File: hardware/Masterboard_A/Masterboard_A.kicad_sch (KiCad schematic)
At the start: 0 parts

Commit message: lv sensor extension board for master
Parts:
- added C11, C5: 220n, Capacitor_SMD:C_1206_3216Metric_Pad1.33x1.80mm_HandSolder, symbol Device:C_Small
- added C14: 10u, Capacitor_SMD:C_1206_3216Metric_Pad1.33x1.80mm_HandSolder, symbol Device:C_Small
- added C15, C3: 100n, Capacitor_SMD:C_1206_3216Metric_Pad1.33x1.80mm_HandSolder, symbol Device:C_Small
- added R7: 49.9k, Resistor_SMD:R_1206_3216Metric_Pad1.30x1.75mm_HandSolder, symbol Device:R_US
- added R8: 100k, Resistor_SMD:R_1206_3216Metric_Pad1.30x1.75mm_HandSolder, symbol Device:R_US
- added SW1: SW_Push, Button_Switch_SMD:SW_SPST_PTS645, symbol Switch:SW_Push
- added U1: MCU-MSM0G3507SPM, PM0064A-IPC_A, symbol zzLocalLibrary:MCU-MSM0G3507SPM
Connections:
- new net: C11.1, C5.1, U1.32 (VCORE)
- new net: R8.2, U1.42 (PA2_ROSC)
- new net +3.3V: C14.1, C15.1, R7.1, U1.40 (VDD)
- new net GND: C11.2, C14.2, C15.2, C3.2, C5.2, R8.1, SW1.2, U1.41 (VSS)
- new net MCU_RST: C3.1, R7.2, SW1.1, U1.38 (RST_N)
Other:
- note added: "MCU reset btn"

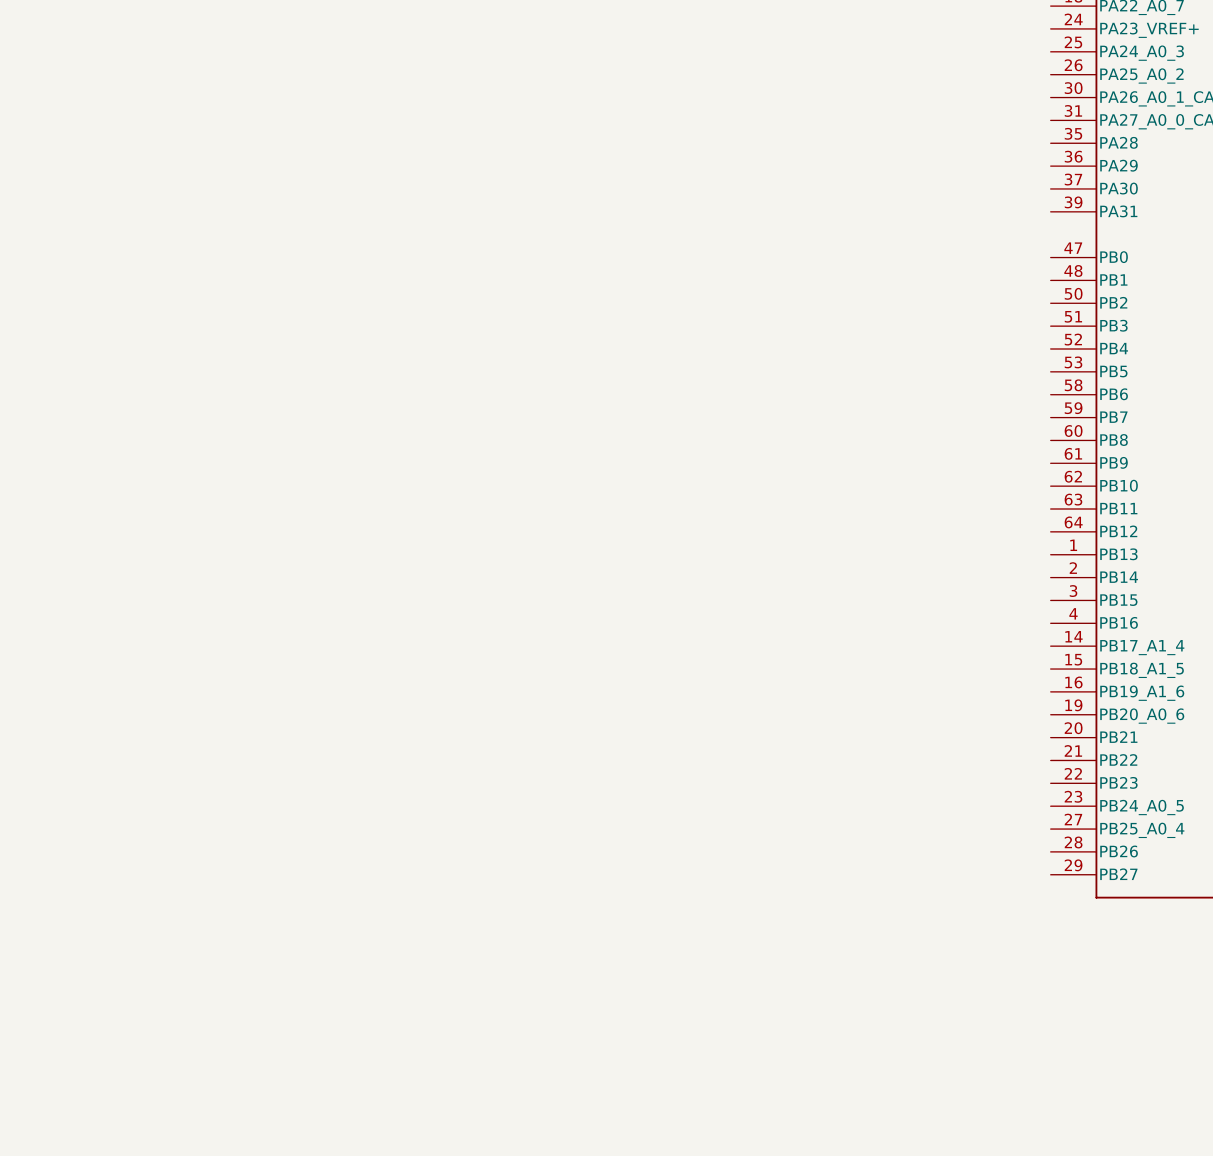
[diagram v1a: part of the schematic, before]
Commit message: Update Masterboard_A.kicad_sch
Pre-charge proof of concept
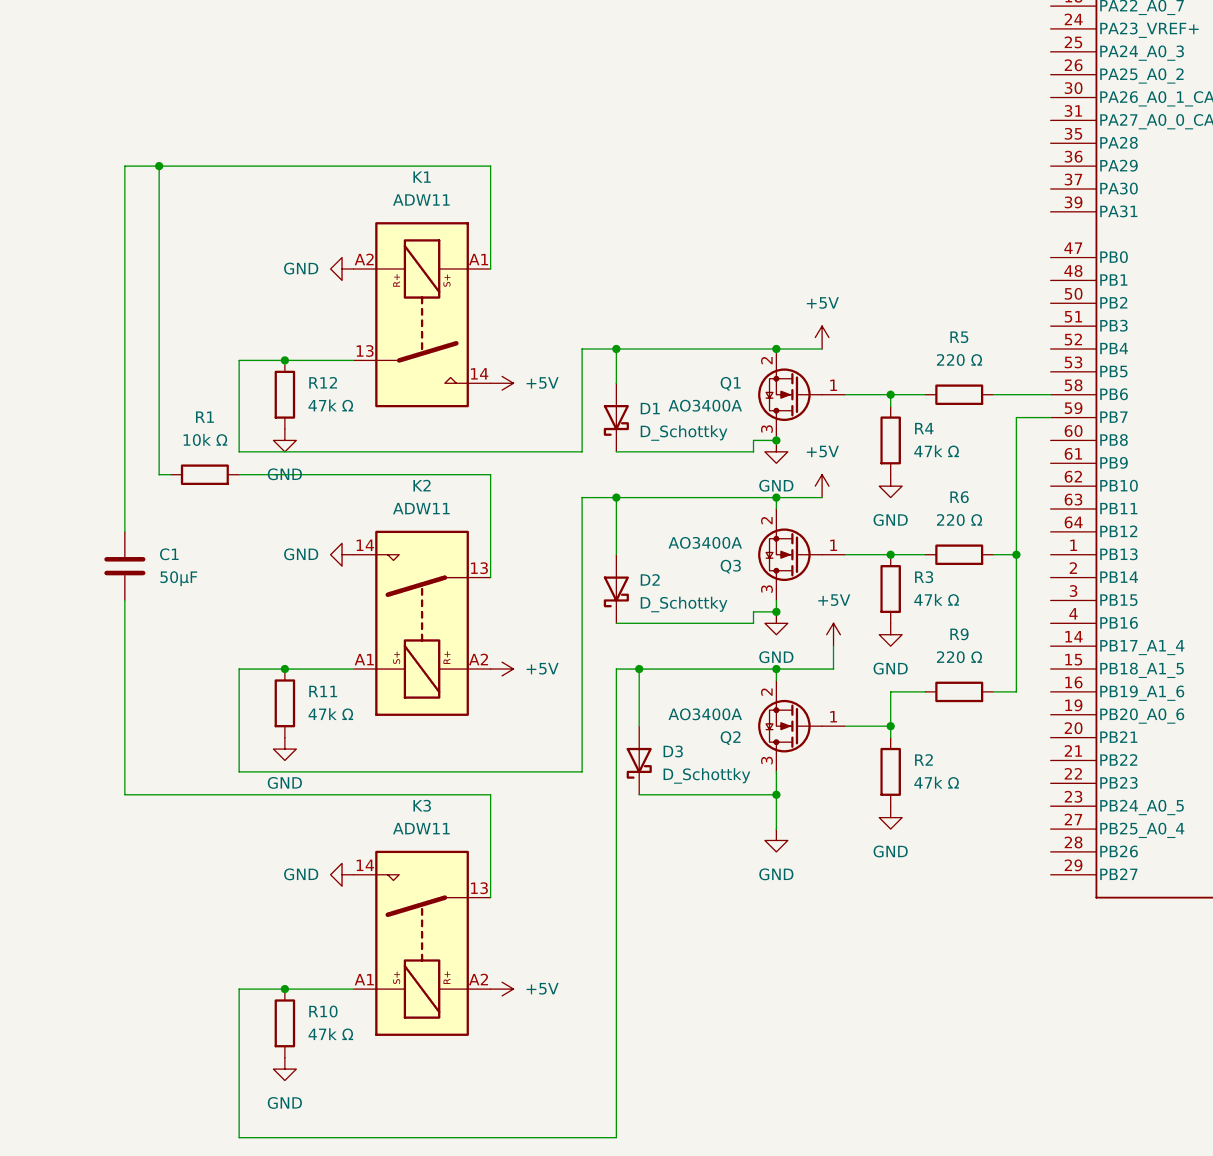
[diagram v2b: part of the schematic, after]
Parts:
- added C1: 50μF, symbol Device:C
- added D1, D2, D3: D_Schottky, symbol Device:D_Schottky
- added K1, K2, K3: ADW11, Relay_THT:Relay_SPST_Panasonic_ADW11, symbol Relay:ADW11
- added Q1, Q2, Q3: AO3400A, Package_TO_SOT_SMD:SOT-23, symbol Transistor_FET:AO3400A
- added R1: 10k Ω, symbol Device:R
- added R10, R11, R12, R2, R3, R4: 47k Ω, symbol Device:R
- added R5, R6, R9: 220 Ω, symbol Device:R
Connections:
- net GND: now also D1.1 (K), D2.1 (K), D3.1 (K), K1.A2, K2.14, K3.14, Q1.3 (D), Q2.3 (D), Q3.3 (D), R10.2, R11.2, R12.2, R2.2, R3.2, R4.2
- net at U1.58 (PB6): now also R5.2
- net at U1.59 (PB7): now also R6.2, R9.2
- new net: Q2.1 (G), R2.1, R9.1
- new net: Q3.1 (G), R3.1, R6.1
- new net: C1.1, K1.A1, R1.1
- new net: K2.13, R1.2
- new net: C1.2, K3.13
- new net: Q1.1 (G), R4.1, R5.1
- new net +5V: D1.2 (A), D2.2 (A), D3.2 (A), K1.13, K1.14, K2.A1, K2.A2, K3.A1, K3.A2, Q1.2 (S), Q2.2 (S), Q3.2 (S), R10.1, R11.1, R12.1

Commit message: masterboardreshuffled
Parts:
- removed C1: 50μF, symbol Device:C
- removed D1, D2, D3: D_Schottky, symbol Device:D_Schottky
- removed K1, K2, K3: ADW11, Relay_THT:Relay_SPST_Panasonic_ADW11, symbol Relay:ADW11
- removed Q1, Q2, Q3: AO3400A, Package_TO_SOT_SMD:SOT-23, symbol Transistor_FET:AO3400A
- removed R1: 10k Ω, symbol Device:R
- removed R10, R11, R12, R2, R3, R4: 47k Ω, symbol Device:R
- removed R5, R6, R9: 220 Ω, symbol Device:R
- removed U1: MCU-MSM0G3507SPM, PM0064A-IPC_A, symbol zzLocalLibrary:MCU-MSM0G3507SPM
- added C12, C13, C7: 220n, Capacitor_SMD:C_1206_3216Metric_Pad1.33x1.80mm_HandSolder, symbol Device:C_Small
- added D3, D4: LED, LED_SMD:LED_0603_1608Metric, symbol Device:LED
- added J1: Conn_01x09_Socket, Connector_PinHeader_2.54mm:PinHeader_1x09_P2.54mm_Vertical, symbol Connector:Conn_01x09_Socket
- added J2: Conn_02x05_Odd_Even, Connector_PinHeader_1.27mm:PinHeader_2x05_P1.27mm_Vertical_SMD, symbol Connector_Generic:Conn_02x05_Odd_Even
- added J3: Conn_01x04_Pin, Connector_PinHeader_2.54mm:PinHeader_1x04_P2.54mm_Vertical, symbol Connector:Conn_01x04_Pin
- added R1, R3: 750, Resistor_SMD:R_1206_3216Metric_Pad1.30x1.75mm_HandSolder, symbol Device:R_US
- added R16, R18: 4.99k, Resistor_SMD:R_1206_3216Metric_Pad1.30x1.75mm_HandSolder, symbol Device:R_US
- added TP14, TP15, TP16, TP2, TP3: TestPoint, TestPoint:TestPoint_Loop_D2.50mm_Drill1.0mm_LowProfile, symbol Connector:TestPoint
- added TP9: TestPoint, TestPoint:TestPoint_THTPad_3.0x3.0mm_Drill1.5mm, symbol Connector:TestPoint
- added U2: MCU-MSM0G3507SPM, zzLocalLibraries-Footprints:MSPM0G3507-64-IPC_A, symbol zzLocalLibrary:MCU-MSM0G3507SPM
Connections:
- net +3.3V: now also C12.1, C13.1, C7.1, R1.2, R16.2, R18.1, U2.40 (VDD)
- net GND: now also C12.2, C13.2, C7.2, D3.1 (K), D4.1 (K), J1.1 (Pin_1), J2.3 (Pin_3), J2.5 (Pin_5), J2.7 (Pin_7), J2.9 (Pin_9), TP14.1, TP15.1, TP16.1, TP9.1, U2.41 (VSS)
- net at C11.1, C5.1: now also TP3.1, U2.32 (VCORE)
- net at R8.2: now also U2.42 (PA2_ROSC)
- net MCU_RST renamed RST_N
- net RST_N: now also J1.6 (Pin_6), J2.10 (Pin_10), U2.38 (RST_N)
- new net: D4.2 (A), R3.2
- new net: D3.2 (A), R1.1
- new net: TP2.1, U2.64 (PB12)
- new net GLV CAN TRX/CAN_H: J3.2 (Pin_2)
- new net GLV CAN TRX/CAN_L: J3.1 (Pin_1)
- new net GLV CAN TRX/CAN_VDD: J3.4 (Pin_4)
- new net GLV CAN TRX/CAN_VSS: J3.3 (Pin_3)
- new net PA10_UART0-TX_XDS: J1.5 (Pin_5), U2.56 (PA10)
- new net PA11_UART0-RX_XDS: J1.4 (Pin_4), U2.57 (PA11)
- new net PA12_CAN_TX: U2.5 (PA12_CAN_TX)
- new net PA13_CAN_RX: U2.6 (PA13_CAN_RX)
- new net PA14: R3.1, U2.7 (PA14)
- new net PA15_I2C1_SCL: R16.1, U2.8 (PA15_A1_0)
- new net PA16_I2C1_SDA: R18.2, U2.9 (PA16_A1_1)
- new net PA18: U2.11 (PA18_A1_3)
- new net PA19_SWDIO: J1.7 (Pin_7), J2.2 (Pin_2), U2.12 (PA19_SWDIO)
- new net PA20_SWCLK: J1.8 (Pin_8), J2.4 (Pin_4), U2.13 (PA20_SWCLK)
- new net PA21_A1_7_VREF-: U2.17 (PA21_A1_7_VREF-)
- new net PA8_UART0-RTS: U2.54 (PA8)
- new net PA9_UART0-CTS: U2.55 (PA9)
- new net XDS_5v_supply: J1.2 (Pin_2)
- new net XDS_TDI: J2.8 (Pin_8)
- new net XDS_TDO_SWO: J2.6 (Pin_6)
- new net XDS_VCC: J2.1 (Pin_1)
- new net onboard 3.3v src: J1.3 (Pin_3)
- no-connect marks 0 -> 45
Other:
- added sheet GLV CAN TRX (GLV CAN TRX.kicad_sch)
- added sheet UART_USB (UART_USB.kicad_sch)
- note added: "*using the XDS debugger"
- note added: "2.1"
- note added: "7/13/2025"
- note added: "EVAL MSPM0G3507 BQ76952"
- note added: "Files at github.com/Gregification/BeeMS"
- note added: "Power source control"
- note added: "Programming"
- note added: "W5500 soon (plz)"
- note added: "ex large"
- note added: "off board comms"
- note added: "reset btn"
- note removed: "MCU reset btn"
- company: FSAE. UTA Racing. -> (none)
- title: BeeMS Master Board A -> (none)
- moved on the sheet: C11, C14, C15, C3, C5, R7, R8, SW1

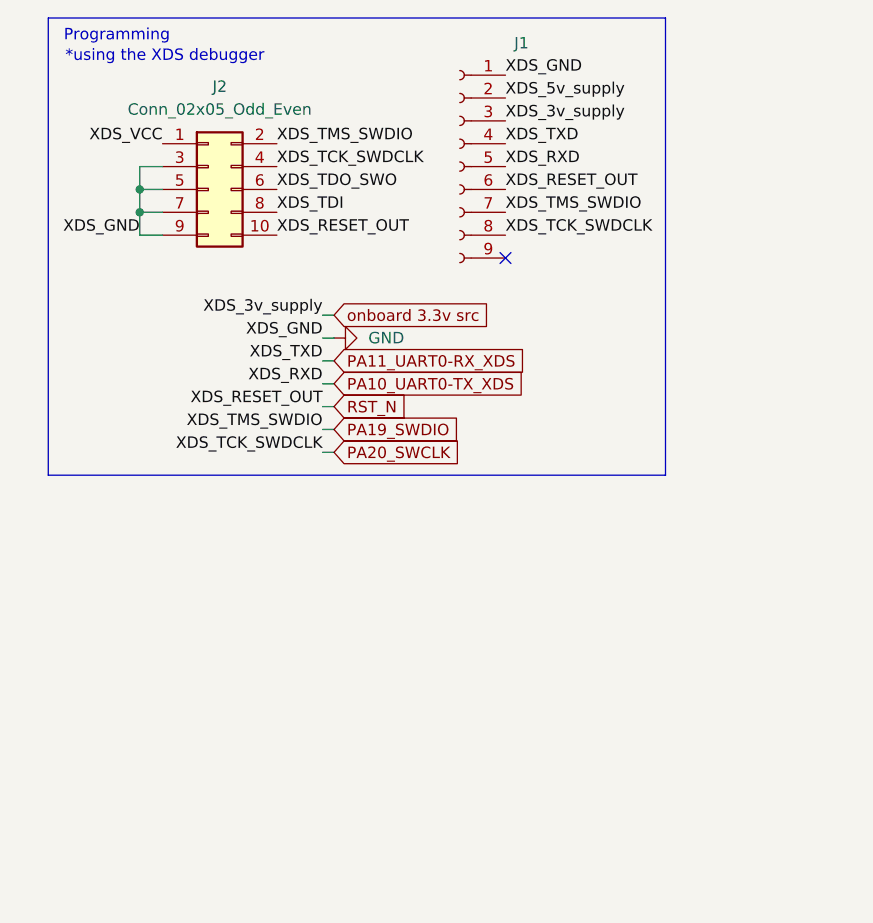
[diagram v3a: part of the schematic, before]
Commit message: added the J2 connections to the MSM board
let me know is this is correct george
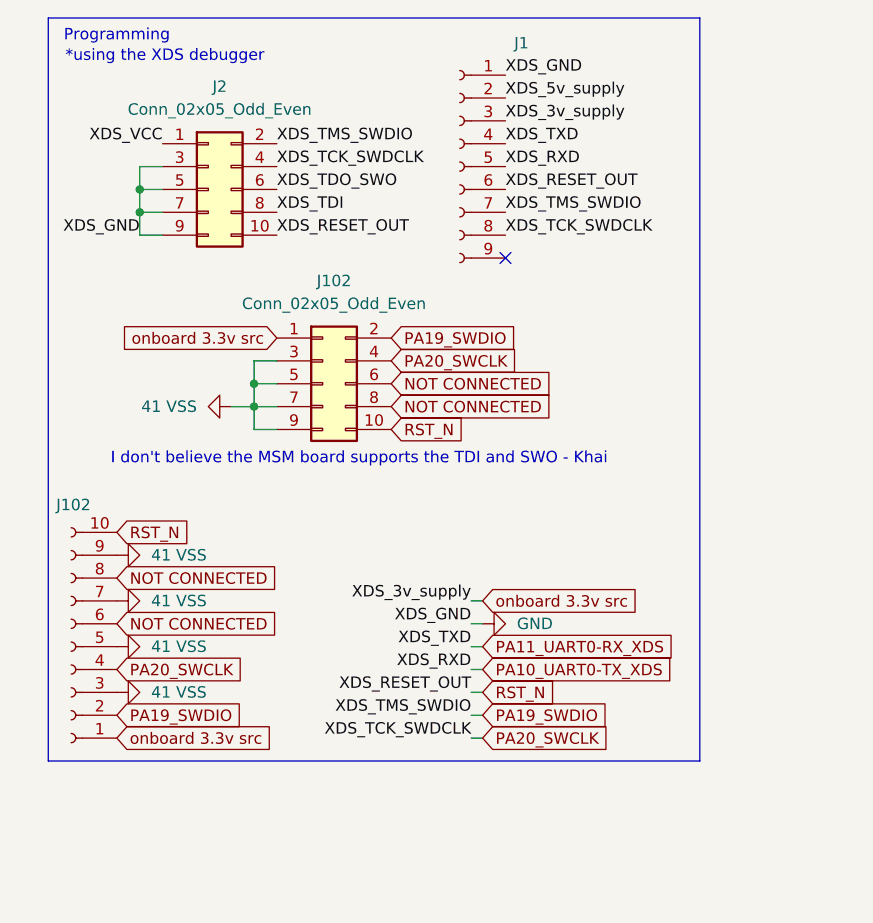
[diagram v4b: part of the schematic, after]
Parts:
- added J102: Conn_01x09_Socket, Connector_PinHeader_2.54mm:PinHeader_1x09_P2.54mm_Vertical, symbol Connector:Conn_01x09_Socket
- added J102: Conn_02x05_Odd_Even, Connector_PinHeader_1.27mm:PinHeader_2x05_P1.27mm_Vertical_SMD, symbol Connector_Generic:Conn_02x05_Odd_Even
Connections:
- net PA19_SWDIO: now also J102.2 (Pin_2), J102.2 (Pin_2)
- net PA20_SWCLK: now also J102.4 (Pin_4), J102.4 (Pin_4)
- net RST_N: now also J102.10 (Pin_10), J102.10 (Pin_9)
- net onboard 3.3v src: now also J102.1 (Pin_1), J102.1 (Pin_1)
- new net 41 VSS: J102.3 (Pin_3), J102.3 (Pin_3), J102.5 (Pin_5), J102.5 (Pin_5), J102.7 (Pin_7), J102.7 (Pin_7), J102.9 (Pin_9), J102.9 (Pin_9)
- new net NOT CONNECTED: J102.6 (Pin_6), J102.6 (Pin_6), J102.8 (Pin_8), J102.8 (Pin_8)
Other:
- note added: "I don't believe the MSM board supports the TDI and SWO - Khai"

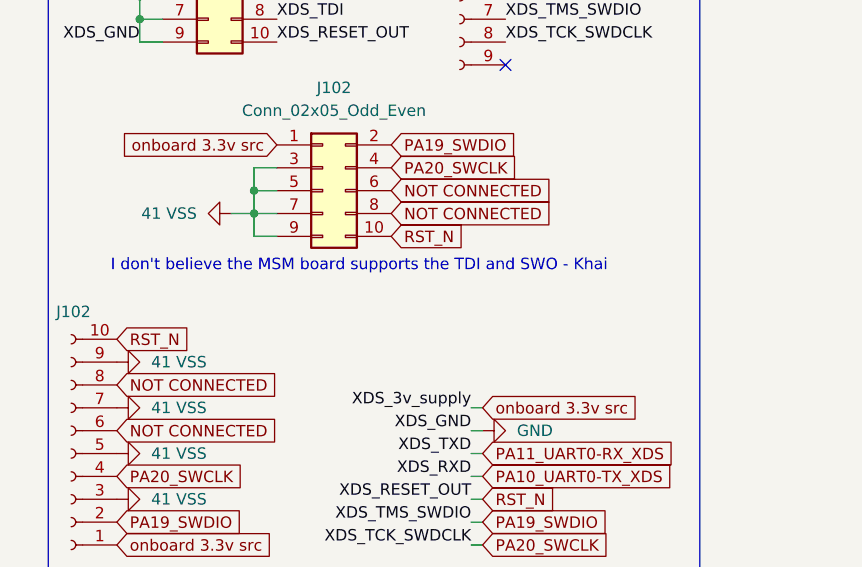
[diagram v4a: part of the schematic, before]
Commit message: Update Masterboard_A.kicad_sch
added additinal support comments
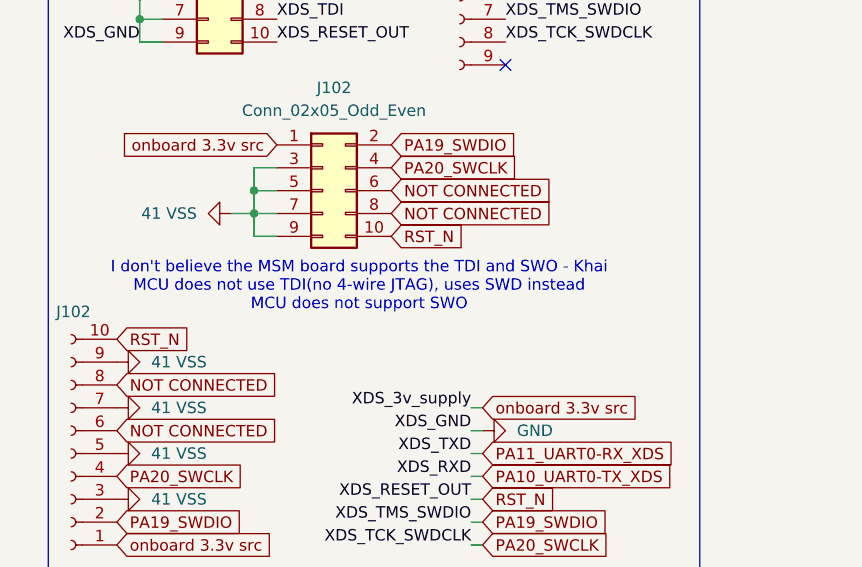
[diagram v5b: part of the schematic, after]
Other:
- note added: "I don't believe the MSM board supports the TDI and SWO - Khai MCU does not use TDI(no 4-wire JTAG), uses SWD instead MCU does not support SWO"
- note removed: "I don't believe the MSM board supports the TDI and SWO - Khai"
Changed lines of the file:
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@@
 		)
 	)
-	(text "I don't believe the MSM board supports the TDI and SWO - Khai"
+	(text "I don't believe the MSM board supports the TDI and SWO - Khai\nMCU does not use TDI(no 4-wire JTAG), uses SWD instead\nMCU does not support SWO"
 		(exclude_from_sim no)
-		(at 47.244 61.722 0)
+		(at 47.244 64.008 0)
 		(effects
 			(font

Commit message: changed
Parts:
- removed J102: Conn_01x09_Socket, Connector_PinHeader_2.54mm:PinHeader_1x09_P2.54mm_Vertical, symbol Connector:Conn_01x09_Socket
- removed J102: Conn_02x05_Odd_Even, Connector_PinHeader_1.27mm:PinHeader_2x05_P1.27mm_Vertical_SMD, symbol Connector_Generic:Conn_02x05_Odd_Even
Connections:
- net XDS_VCC is gone; now on net onboard 3.3v src: J2.1 (Pin_1)
- no-connect marks 45 -> 47
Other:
- note removed: "I don't believe the MSM board supports the TDI and SWO - Khai MCU does not use TDI(no 4-wire JTAG), uses SWD instead MCU does not support SWO"
